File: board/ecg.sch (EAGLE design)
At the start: 10 parts, among them U1 ADAS1000, Y1 8.192MHz

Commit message: do some power work
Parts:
- added C6, C7: 10uF, scono:CAP0603-CAP
- added IC2: MIC5504-3.3, scono:MIC5504-3.3
- added J1: USB_MICRO, scono:USB_MICRO
- C4, C5: value 0.1uF -> 18pF
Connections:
- net N$2 renamed RLD
- new net 3.3V: C6.2, C7.2, IC2.3.3V, U1.AVDD, U1.IOVDD
- new net ADAS_CS: U1.!CS
- new net ADAS_MISO: U1.MISO
- new net ADAS_MOSI: U1.MOSI
- new net LA: U1.LA
- new net LL: U1.LL
- new net N$12: U1.!DRDY
- new net PD: U1.!PD
- new net RA: U1.RA
- new net RESET: U1.!RESET
- new net SCLK: U1.SCLK
- new net V1: U1.V1
- new net V2: U1.V2
- new net VCC: IC2.VIN, J1.VCC
- net GND: now also C6.1, C7.1, J1.GND, U1.AGND, U1.DGND, U1.REFGND
- net N$6: now also U1.XTAL1; no longer U1.XTAL2
- net N$7: now also U1.XTAL2; no longer U1.CLK_IO

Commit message: do tons of library work and nearly wrap up schematic
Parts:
- removed IC2: MIC5504-3.3, scono:MIC5504-3.3
- added C10: 22uF, scono:CAP0603-CAP
- added C11: 1.0pF, scono:CAP0603-CAP
- added C8: 10uF, scono:CAP0603-CAP
- added C9: 0.1uF, scono:CAP0603-CAP
- added IC1: SC189C, scono:SC189C
- added L1: 1uH, scono:IND
- added L2: 3.6nH, scono:IND0402
- added U2: CC3200MOD, scono:CC3200MOD
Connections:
- new net N$2: IC1.LX, L1.2
- new net N$8: L2.1, U2.RF_BG
- new net N$9: C11.2, L2.2
- net 3.3V: now also C10.2, C8.1, C9.1, IC1.3.3V, L1.1, U2.VBAT_DCDC_ANA, U2.VBAT_DCDC_DIG_IO, U2.VBAT_DCDC_PA; no longer IC2.3.3V
- net ADAS_CS: now also U2.GPIO17
- net ADAS_MISO: now also U2.GPIO15
- net ADAS_MOSI: now also U2.GPIO16
- net GND: now also C10.1, C11.1, C8.2, C9.2, IC1.GND
- net SCLK: now also U2.GPIO14
- net VCC: now also IC1.EN, IC1.VIN; no longer IC2.VIN
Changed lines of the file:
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@@
 <layers>
 <layer number="1" name="Top" color="4" fill="1" visible="no" active="no"/>
+<layer number="2" name="Route2" color="1" fill="3" visible="no" active="no"/>
+<layer number="3" name="Route3" color="4" fill="3" visible="no" active="no"/>
+<layer number="4" name="Route4" color="1" fill="4" visible="no" active="no"/>
+<layer number="5" name="Route5" color="4" fill="4" visible="no" active="no"/>
+<layer number="6" name="Route6" color="1" fill="8" visible="no" active="no"/>
+<layer number="7" name="Route7" color="4" fill="8" visible="no" active="no"/>
+<layer number="8" name="Route8" color="1" fill="2" visible="no" active="no"/>
+<layer number="9" name="Route9" color="4" fill="2" visible="no" active="no"/>
+<layer number="10" name="Route10" color="1" fill="7" visible="no" active="no"/>
+<layer number="11" name="Route11" color="4" fill="7" visible="no" active="no"/>
+<layer number="12" name="Route12" color="1" fill="5" visible="no" active="no"/>
+<layer number="13" name="Route13" color="4" fill="5" visible="no" active="no"/>
+<layer number="14" name="Route14" color="1" fill="6" visible="no" active="no"/>
+<layer number="15" name="Route15" color="4" fill="6" visible="no" active="no"/>
 <layer number="16" name="Bottom" color="1" fill="1" visible="no" active="no"/>
 <layer number="17" name="Pads" color="2" fill="1" visible="no" active="no"/>
@@
 <attribute name="SUBSYSTEM_NAME" value="Power"/>
 </part>
-<part name="IC2" library="scono" deviceset="MIC5504-3.3" device=""/>
 <part name="J1" library="scono" deviceset="USB_MICRO" device=""/>
 <part name="SUPPLY10" library="scono" deviceset="VCC" device=""/>
@@
 <part name="SUPPLY13" library="scono" deviceset="VCC" device=""/>
 <part name="U$2" library="scono" deviceset="3.3V" device=""/>
+<part name="FRAME3" library="scono" deviceset="FRAME_SCHEMATIC" device="">
+<attribute name="AUTHOR" value="S.Ono"/>
+<attribute name="REV" value="A"/>
+<attribute name="SUBSYSTEM_NAME" value="CC3200MOD"/>
+</part>
+<part name="U2" library="scono" deviceset="CC3200MOD" device=""/>
+<part name="U$1" library="scono" deviceset="3.3V" device=""/>
+<part name="C8" library="scono" deviceset="CAP" device="0603-CAP" value="10uF"/>
+<part name="C9" library="scono" deviceset="CAP" device="0603-CAP" value="0.1uF"/>
+<part name="SUPPLY12" library="scono" deviceset="GND" device=""/>
+<part name="SUPPLY14" library="scono" deviceset="GND" device=""/>
+<part name="IC1" library="scono" deviceset="SC189C" device=""/>
+<part name="SUPPLY15" library="scono" deviceset="GND" device=""/>
+<part name="L1" library="scono" deviceset="IND" device="" value="1uH"/>
+<part name="C10" library="scono" deviceset="CAP" device="0603-CAP" value="22uF"/>
+<part name="SUPPLY16" library="scono" deviceset="GND" device=""/>
+<part name="L2" library="scono" deviceset="IND" device="0402" value="3.6nH"/>
+<part name="C11" library="scono" deviceset="CAP" device="0603-CAP" value="1.0pF"/>
+<part name="SUPPLY17" library="scono" deviceset="GND" device=""/>
 </parts>
 <sheets>
@@
 </instance>
 <instance part="FRAME2" gate="G$2" x="147.32" y="0"/>
-<instance part="IC2" gate="G$1" x="99.06" y="83.82"/>
 <instance part="J1" gate="G$1" x="35.56" y="86.36"/>
 <instance part="SUPPLY10" gate="G$1" x="53.34" y="91.44"/>
 <instance part="SUPPLY11" gate="GND" x="53.34" y="78.74"/>
-<instance part="SUPPLY13" gate="G$1" x="86.36" y="86.36"/>
-<instance part="U$2" gate="G$1" x="114.3" y="86.36"/>
+<instance part="SUPPLY13" gate="G$1" x="83.82" y="88.9"/>
+<instance part="U$2" gate="G$1" x="124.46" y="88.9"/>
+<instance part="IC1" gate="G$1" x="99.06" y="83.82"/>
+<instance part="SUPPLY15" gate="GND" x="99.06" y="71.12"/>
+<instance part="L1" gate="A" x="109.22" y="88.9"/>
+<instance part="C10" gate="G$1" x="124.46" y="81.28" rot="R90"/>
+<instance part="SUPPLY16" gate="GND" x="124.46" y="76.2"/>
 </instances>
 <busses>
@@
 <wire x1="45.72" y1="81.28" x2="53.34" y2="81.28" width="0.1524" layer="91"/>
 </segment>
+<segment>
+<pinref part="IC1" gate="G$1" pin="GND"/>
+<pinref part="SUPPLY15" gate="GND" pin="GND"/>
+</segment>
+<segment>
+<pinref part="C10" gate="G$1" pin="1"/>
+<pinref part="SUPPLY16" gate="GND" pin="GND"/>
+</segment>
 </net>
 <net name="VCC" class="0">
@@
 <segment>
 <pinref part="SUPPLY13" gate="G$1" pin="VCC"/>
-<pinref part="IC2" gate="G$1" pin="VIN"/>
-<wire x1="86.36" y1="86.36" x2="88.9" y2="86.36" width="0.1524" layer="91"/>
+<pinref part="IC1" gate="G$1" pin="VIN"/>
+<wire x1="83.82" y1="88.9" x2="88.9" y2="88.9" width="0.1524" layer="91"/>
+<pinref part="IC1" gate="G$1" pin="EN"/>
+<wire x1="88.9" y1="88.9" x2="88.9" y2="83.82" width="0.1524" layer="91"/>
 </segment>
 </net>
 <net name="3.3V" class="0">
 <segment>
-<pinref part="IC2" gate="G$1" pin="3.3V"/>
 <pinref part="U$2" gate="G$1" pin="3.3V"/>
-<wire x1="109.22" y1="86.36" x2="114.3" y2="86.36" width="0.1524" layer="91"/>
-</segment>
-</net>
+<pinref part="L1" gate="A" pin="1"/>
+<pinref part="C10" gate="G$1" pin="2"/>
+<wire x1="124.46" y1="88.9" x2="124.46" y2="83.82" width="0.1524" layer="91"/>
+<pinref part="IC1" gate="G$1" pin="3.3V"/>
+<wire x1="124.46" y1="83.82" x2="109.22" y2="83.82" width="0.1524" layer="91"/>
+</segment>
+</net>
+<net name="N$2" class="0">
+<segment>
+<pinref part="IC1" gate="G$1" pin="LX"/>
+<pinref part="L1" gate="A" pin="2"/>
+</segment>
+</net>
+</nets>
+</sheet>
+<sheet>
+<plain>
+</plain>
+<instances>
+<instance part="FRAME3" gate="G$1" x="0" y="0">
+<attribute name="SUBSYSTEM_NAME" x="0" y="0" size="1.778" layer="96" display="off"/>
+<attribute name="REV" x="0" y="0" size="1.778" layer="96" display="off"/>
+<attribute name="AUTHOR" x="0" y="0" size="1.778" layer="96" display="off"/>
+</instance>
+<instance part="FRAME3" gate="G$2" x="147.32" y="0"/>
+<instance part="U2" gate="G$1" x="132.08" y="91.44"/>
+<instance part="U$1" gate="G$1" x="104.14" y="111.76"/>
+<instance part="C8" gate="G$1" x="99.06" y="111.76" rot="R180"/>
+<instance part="C9" gate="G$1" x="99.06" y="106.68" rot="R180"/>
+<instance part="SUPPLY12" gate="GND" x="93.98" y="111.76" rot="R270"/>
+<instance part="SUPPLY14" gate="GND" x="93.98" y="106.68" rot="R270"/>
+<instance part="L2" gate="A" x="83.82" y="134.62"/>
+<instance part="C11" gate="G$1" x="78.74" y="132.08" rot="R90"/>
+<instance part="SUPPLY17" gate="GND" x="78.74" y="127"/>
+</instances>
+<busses>
+</busses>
+<nets>
+<net name="GND" class="0">
+<segment>
+<pinref part="C8" gate="G$1" pin="2"/>
+<pinref part="SUPPLY12" gate="GND" pin="GND"/>
+</segment>
+<segment>
+<pinref part="C9" gate="G$1" pin="2"/>
+<pinref part="SUPPLY14" gate="GND" pin="GND"/>
+</segment>
+<segment>
+<pinref part="C11" gate="G$1" pin="1"/>
+<pinref part="SUPPLY17" gate="GND" pin="GND"/>
+</segment>
+</net>
+<net name="3.3V" class="0">
+<segment>
+<pinref part="C8" gate="G$1" pin="1"/>
+<pinref part="U$1" gate="G$1" pin="3.3V"/>
+<wire x1="101.6" y1="111.76" x2="104.14" y2="111.76" width="0.1524" layer="91"/>
+<pinref part="U2" gate="G$1" pin="VBAT_DCDC_DIG_IO"/>
+<wire x1="104.14" y1="111.76" x2="109.22" y2="111.76" width="0.1524" layer="91"/>
+<pinref part="U2" gate="G$1" pin="VBAT_DCDC_ANA"/>
+<wire x1="109.22" y1="111.76" x2="109.22" y2="109.22" width="0.1524" layer="91"/>
+<pinref part="U2" gate="G$1" pin="VBAT_DCDC_PA"/>
+<wire x1="109.22" y1="109.22" x2="109.22" y2="106.68" width="0.1524" layer="91"/>
+<pinref part="C9" gate="G$1" pin="1"/>
+<wire x1="109.22" y1="106.68" x2="101.6" y2="106.68" width="0.1524" layer="91"/>
+</segment>
+</net>
+<net name="SCLK" class="0">
+<segment>
+<pinref part="U2" gate="G$1" pin="GPIO14"/>
+<wire x1="152.4" y1="88.9" x2="157.48" y2="88.9" width="0.1524" layer="91"/>
+<label x="157.48" y="88.9" size="1.778" layer="95"/>
+</segment>
+</net>
+<net name="ADAS_MISO" class="0">
+<segment>
+<pinref part="U2" gate="G$1" pin="GPIO15"/>
+<wire x1="152.4" y1="86.36" x2="157.48" y2="86.36" width="0.1524" layer="91"/>
+<label x="157.48" y="86.36" size="1.778" layer="95"/>
+</segment>
+</net>
+<net name="ADAS_MOSI" class="0">
+<segment>
+<pinref part="U2" gate="G$1" pin="GPIO16"/>
+<wire x1="152.4" y1="83.82" x2="157.48" y2="83.82" width="0.1524" layer="91"/>
+<label x="157.48" y="83.82" size="1.778" layer="95"/>
+</segment>
+</net>
+<net name="ADAS_CS" class="0">
+<segment>
+<pinref part="U2" gate="G$1" pin="GPIO17"/>
+<wire x1="152.4" y1="81.28" x2="157.48" y2="81.28" width="0.1524" layer="91"/>
+<label x="157.48" y="81.28" size="1.778" layer="95"/>
+</segment>
+</net>
+<net name="N$8" class="0">
+<segment>
+<pinref part="U2" gate="G$1" pin="RF_BG"/>
+<pinref part="L2" gate="A" pin="1"/>
+<wire x1="109.22" y1="124.46" x2="109.22" y2="134.62" width="0.1524" layer="91"/>
+<wire x1="109.22" y1="134.62" x2="99.06" y2="134.62" width="0.1524" layer="91"/>
+</segment>
+</net>
+<net name="N$9" class="0">
+<segment>
+<pinref part="L2" gate="A" pin="2"/>
+<pinref part="C11" gate="G$1" pin="2"/>
+<wire x1="83.82" y1="134.62" x2="78.74" y2="134.62" width="0.1524" layer="91"/>
+</segment>
+</net>

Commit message: make progress with the board
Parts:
- added D16: RED, scono:LED0603
- added D17: BLUE, scono:LED0603
- added D18: GREEN, scono:LED0603
- added D19: YELLOW, scono:LED0603
- added D20: WHITE, scono:LED0603
- added E1: (no value), scono:AH316M245001-T
- added J2: PROG, scono:CONN_04
- added J3: JTAG, scono:CONN_04
- added R19, R20, R21, R22, R23: 330, BEST_Custom:R-US_R0402
- added R4: 2.7K, BEST_Custom:R-US_R0402
- added R5: 100K, BEST_Custom:R-US_R0402
- added S1: (no value), scono:DP3T
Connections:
- net N$8 renamed RF_BG
- removed net N$12: U1.!DRDY
- new net BLUE: R20.2, U2.GPIO4
- new net GPIO1: J2.2, U2.GPIO1
- new net GPIO2: J2.3, U2.GPIO2
- new net GREEN: R21.2, U2.GPIO5
- new net N$10: J3.2, U2.JTAG_TDO
- new net N$11: J3.1, U2.JTAG_TDI
- new net N$15: S1.4
- new net N$19: S1.8
- new net N$24: D16.A, R19.1
- new net N$25: D17.A, R20.1
- new net N$26: D18.A, R21.1
- new net N$27: D19.A, R22.1
- new net N$28: D20.A, R23.1
- new net N$8: J3.4, R5.1, U2.JTAG_TCK
- new net NC_GND: S1.6
- new net NC_PWR: S1.2
- new net NRESET: J2.1, U2.NRESET
- new net RF_IN: C11.2, E1.INPUT, L2.2
- new net SOP2: J2.4, R4.1, U2.TCXO_EN/SOP2
- new net USB: J1.VCC, S1.1
- new net USB_GND: J1.GND, S1.5
- new net WHITE: R23.2, U2.GPIO7
- new net YELLOW: R22.2, U2.GPIO6
- net 3.3V: now also R19.2
- net GND: now also D16.C, D17.C, D18.C, D19.C, D20.C, E1.GND, R4.2, R5.2, S1.7, U2.GND; no longer J1.GND
- net N$9: now also J3.3, U2.JTAG_TMS; no longer C11.2, L2.2
- net VCC: now also S1.3; no longer J1.VCC
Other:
- note added: "GND"
- note added: "PWR"

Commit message: finish bom and replace 0402
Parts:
- added C12: 10uF, scono:CAP0603-CAP
- added GND: (no value), scono:CONN_02
- added J4: 2_PIN_JST-XH, scono:2_PIN_JST-XH
- added UART: PROG, scono:CONN_04
- added X1: FH12-32S-0.5SH, scono:FH12-32S-0.5SH
- R4: value 2.7K -> 2.7k; device BEST_Custom:R-US_R0402 -> scono:R-US_R0603
- R5: value 100K -> 100k; device BEST_Custom:R-US_R0402 -> scono:R-US_R0603
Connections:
- removed net N$15: S1.4
- removed net N$19: S1.8
- new net BAT+: J4.2, S1.1
- new net BAT-: J4.1, S1.5
- new net UART0_RX: U2.GPIO13, UART.2
- new net UART0_TX: U2.GPIO12, UART.3
- net 3.3V: now also C12.2, UART.1
- net BLUE: now also U2.GPIO7; no longer U2.GPIO4
- net GND: now also C12.1, GND.1, GND.2, UART.4, X1-28.1
- net GREEN: now also U2.GPIO6; no longer U2.GPIO5
- net LA: now also X1-4.1
- net LL: now also X1-8.1
- net RA: now also X1-12.1
- net RLD: now also X1-24.1
- net USB: now also S1.4; no longer S1.1
- net USB_GND: now also S1.8; no longer S1.5
- net V1: now also X1-16.1
- net V2: now also X1-20.1
- net WHITE: now also U2.GPIO4; no longer U2.GPIO7
- net YELLOW: now also U2.GPIO5; no longer U2.GPIO6
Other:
- moved on the sheet: C10, IC1, J1, L1, R4, R5, S1

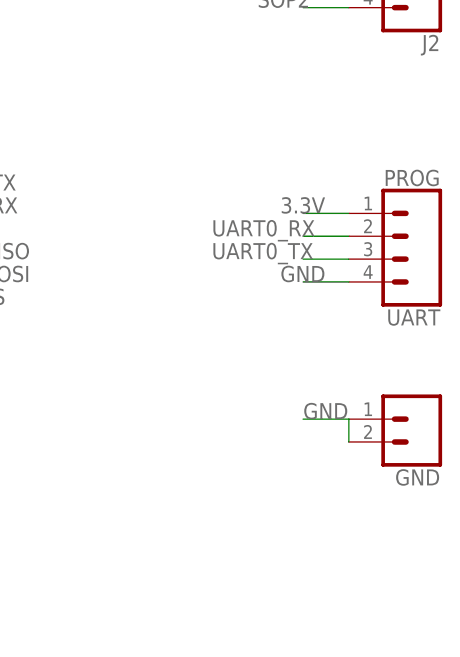
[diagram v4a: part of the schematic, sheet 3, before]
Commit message: make sure the pinouts are same as te board
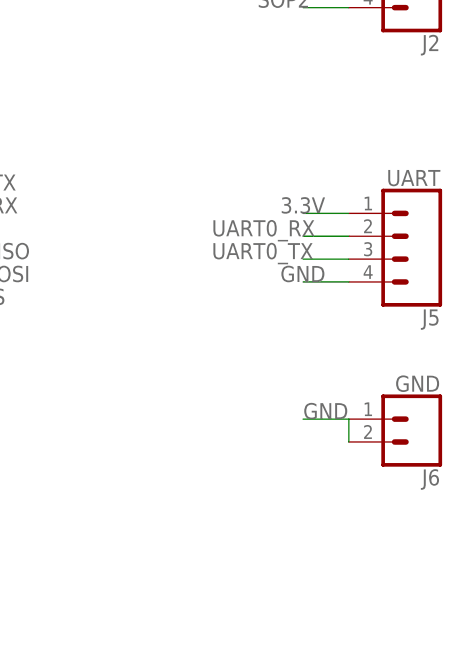
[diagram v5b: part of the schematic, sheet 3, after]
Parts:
- J5: value PROG -> UART
- J6: value (none) -> GND
- renumbered GND to J6, UART to J5
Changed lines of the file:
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@@
 <part name="U$3" library="scono" deviceset="3.3V" device=""/>
 <part name="J4" library="scono" deviceset="2_PIN_JST-XH" device=""/>
-<part name="UART" library="scono" deviceset="CONN_04" device="" package3d_urn="urn:adsk.eagle:package:38085/1" value="PROG"/>
-<part name="GND" library="scono" deviceset="CONN_02" device="" package3d_urn="urn:adsk.eagle:package:38039/1"/>
+<part name="J5" library="scono" deviceset="CONN_04" device="" package3d_urn="urn:adsk.eagle:package:38085/1" value="UART"/>
+<part name="J6" library="scono" deviceset="CONN_02" device="" package3d_urn="urn:adsk.eagle:package:38039/1" value="GND"/>
 </parts>
 <sheets>
@@
 <instance part="R5" gate="G$1" x="71.12" y="91.44" rot="R270"/>
 <instance part="SUPPLY23" gate="GND" x="71.12" y="83.82"/>
-<instance part="UART" gate="G$1" x="210.82" y="88.9" rot="R180"/>
-<instance part="GND" gate="G$1" x="213.36" y="68.58" rot="R180"/>
+<instance part="J5" gate="G$1" x="210.82" y="88.9" rot="R180"/>
+<instance part="J6" gate="G$1" x="213.36" y="68.58" rot="R180"/>
 </instances>
 <busses>
@@
 </segment>
 <segment>
-<pinref part="GND" gate="G$1" pin="1"/>
+<pinref part="J6" gate="G$1" pin="1"/>
 <wire x1="200.66" y1="68.58" x2="205.74" y2="68.58" width="0.1524" layer="91"/>
-<pinref part="GND" gate="G$1" pin="2"/>
+<pinref part="J6" gate="G$1" pin="2"/>
 <wire x1="205.74" y1="68.58" x2="205.74" y2="66.04" width="0.1524" layer="91"/>
 <label x="200.66" y="68.58" size="1.778" layer="95"/>
 </segment>
 <segment>
-<pinref part="UART" gate="G$1" pin="4"/>
+<pinref part="J5" gate="G$1" pin="4"/>
 <wire x1="205.74" y1="83.82" x2="200.66" y2="83.82" width="0.1524" layer="91"/>
 <label x="198.12" y="83.82" size="1.778" layer="95"/>
@@
 </segment>
 <segment>
-<pinref part="UART" gate="G$1" pin="1"/>
+<pinref part="J5" gate="G$1" pin="1"/>
 <wire x1="205.74" y1="91.44" x2="200.66" y2="91.44" width="0.1524" layer="91"/>
 <label x="198.12" y="91.44" size="1.778" layer="95"/>
@@
 </segment>
 <segment>
-<pinref part="UART" gate="G$1" pin="3"/>
+<pinref part="J5" gate="G$1" pin="3"/>
 <wire x1="205.74" y1="86.36" x2="200.66" y2="86.36" width="0.1524" layer="91"/>
 <label x="190.5" y="86.36" size="1.778" layer="95"/>
@@
 </segment>
 <segment>
-<pinref part="UART" gate="G$1" pin="2"/>
+<pinref part="J5" gate="G$1" pin="2"/>
 <wire x1="205.74" y1="88.9" x2="200.66" y2="88.9" width="0.1524" layer="91"/>
 <label x="190.5" y="88.9" size="1.778" layer="95"/>

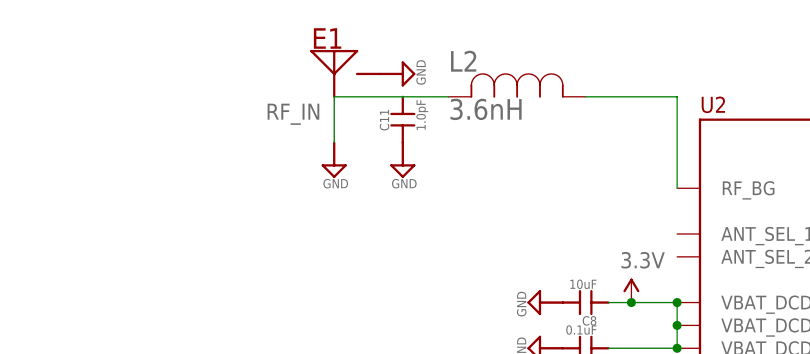
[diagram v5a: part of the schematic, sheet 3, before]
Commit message: fix antenna
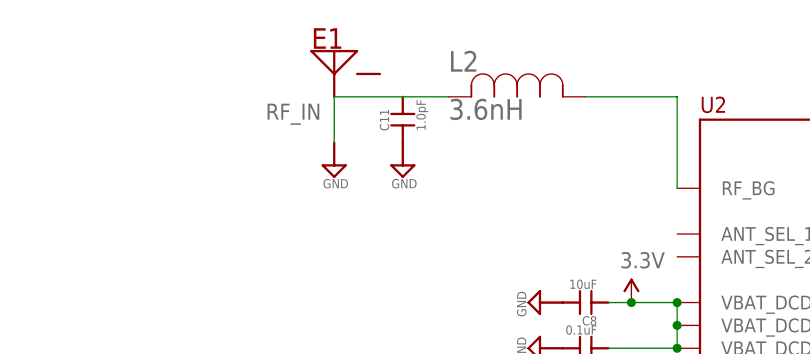
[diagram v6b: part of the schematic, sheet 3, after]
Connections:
- net GND: no longer E1.GND
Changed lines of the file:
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@@
 <part name="E1" library="scono" deviceset="AH316M245001-T" device=""/>
 <part name="SUPPLY18" library="scono" deviceset="GND" device=""/>
-<part name="SUPPLY19" library="scono" deviceset="GND" device=""/>
 <part name="SUPPLY20" library="scono" deviceset="GND" device=""/>
 <part name="D16" library="scono" deviceset="LED" device="0603" value="RED"/>
@@
 <instance part="E1" gate="G$1" x="71.12" y="134.62"/>
 <instance part="SUPPLY18" gate="GND" x="71.12" y="127"/>
-<instance part="SUPPLY19" gate="GND" x="78.74" y="137.16" rot="R90"/>
 <instance part="SUPPLY20" gate="GND" x="106.68" y="71.12"/>
 <instance part="D16" gate="G$1" x="40.64" y="27.94"/>
@@
 </segment>
 <segment>
-<pinref part="E1" gate="G$1" pin="GND"/>
-<pinref part="SUPPLY19" gate="GND" pin="GND"/>
-</segment>
-<segment>

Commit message: fix cs pin and add more links
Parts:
- added J7: SPI, scono:CONN_04
- added R6: 10k, scono:R-US_R0603
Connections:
- net ADAS_CS: now also J7.1, R6.2
- net ADAS_MISO: now also J7.4
- net ADAS_MOSI: now also J7.2
- net GND: now also R6.1
- net SCLK: now also J7.3

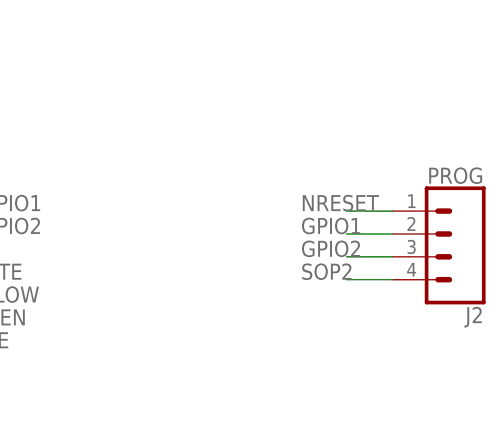
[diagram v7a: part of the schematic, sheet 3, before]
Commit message: make sure pullup for !CS
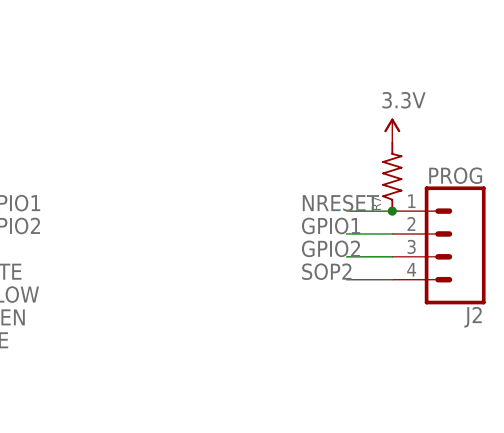
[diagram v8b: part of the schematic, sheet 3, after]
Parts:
- added R7: (no value), scono:R-US_R0603
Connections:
- net 3.3V: now also R6.1, R7.2
- net GND: no longer R6.1
- net NRESET: now also R7.1
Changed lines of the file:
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@@
 <part name="J7" library="scono" deviceset="CONN_04" device="" package3d_urn="urn:adsk.eagle:package:38085/1" value="SPI"/>
 <part name="R6" library="scono" deviceset="R-US_" device="R0603" value="10k"/>
-<part name="SUPPLY19" library="scono" deviceset="GND" device=""/>
+<part name="R7" library="scono" deviceset="R-US_" device="R0603"/>
+<part name="U$4" library="scono" deviceset="3.3V" device=""/>
 </parts>
 <sheets>
@@
 <attribute name="NAME" x="46.99" y="104.14" size="1.016" layer="95" rot="R90"/>
 <attribute name="VALUE" x="49.53" y="104.14" size="1.016" layer="96" rot="R90" align="top-left"/>
-</instance>
-<instance part="SUPPLY19" gate="GND" x="48.26" y="101.6" smashed="yes">
-<attribute name="VALUE" x="46.99" y="99.06" size="1.016" layer="96"/>
 </instance>
 </instances>
@@
 <pinref part="C12" gate="G$1" pin="1"/>
 <pinref part="SUPPLY25" gate="GND" pin="GND"/>
-</segment>
-<segment>
-<pinref part="R6" gate="G$1" pin="1"/>
-<pinref part="SUPPLY19" gate="GND" pin="GND"/>
 </segment>
 </net>
@@
 <pinref part="U$3" gate="G$1" pin="3.3V"/>
 </segment>
+<segment>
+<pinref part="R6" gate="G$1" pin="1"/>
+<wire x1="48.26" y1="104.14" x2="48.26" y2="101.6" width="0.1524" layer="91"/>
+</segment>
 </net>
 <net name="ADAS_CS" class="0">
@@
 <attribute name="VALUE" x="215.9" y="73.406" size="1.778" layer="96" font="vector" rot="R180"/>
 <attribute name="NAME" x="215.9" y="62.992" size="1.778" layer="95" font="vector" rot="R180"/>
+</instance>
+<instance part="R7" gate="G$1" x="205.74" y="127" smashed="yes" rot="R90">
+<attribute name="NAME" x="204.47" y="121.92" size="1.016" layer="95" rot="R90"/>
+<attribute name="VALUE" x="207.01" y="121.92" size="1.016" layer="96" rot="R90" align="top-left"/>
+</instance>
+<instance part="U$4" gate="G$1" x="205.74" y="129.54" smashed="yes">
+<attribute name="VALUE" x="204.47" y="133.35" size="1.778" layer="96"/>
 </instance>
 </instances>
@@
 <label x="198.12" y="91.44" size="1.778" layer="95"/>
 </segment>
+<segment>
+<pinref part="R7" gate="G$1" pin="2"/>
+<pinref part="U$4" gate="G$1" pin="3.3V"/>
+</segment>
 </net>
 <net name="SCLK" class="0">
@@
 <wire x1="205.74" y1="121.92" x2="200.66" y2="121.92" width="0.1524" layer="91"/>
 <label x="195.58" y="121.92" size="1.778" layer="95"/>
-</segment>
-</net>
+<pinref part="R7" gate="G$1" pin="1"/>
+<junction x="205.74" y="121.92"/>
+</segment>
+</net>
